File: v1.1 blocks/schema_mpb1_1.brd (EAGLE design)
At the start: 70.8 x 85.3 mm, 78 parts, among them IC1 CP2102, Q1 8M, Q2 32.768kHz, U1 NCP1117ST33T3G, U2 NCP1117ST50T3G, X2 PN61729-S, X5 POWERSUPPLY_DC21MMX

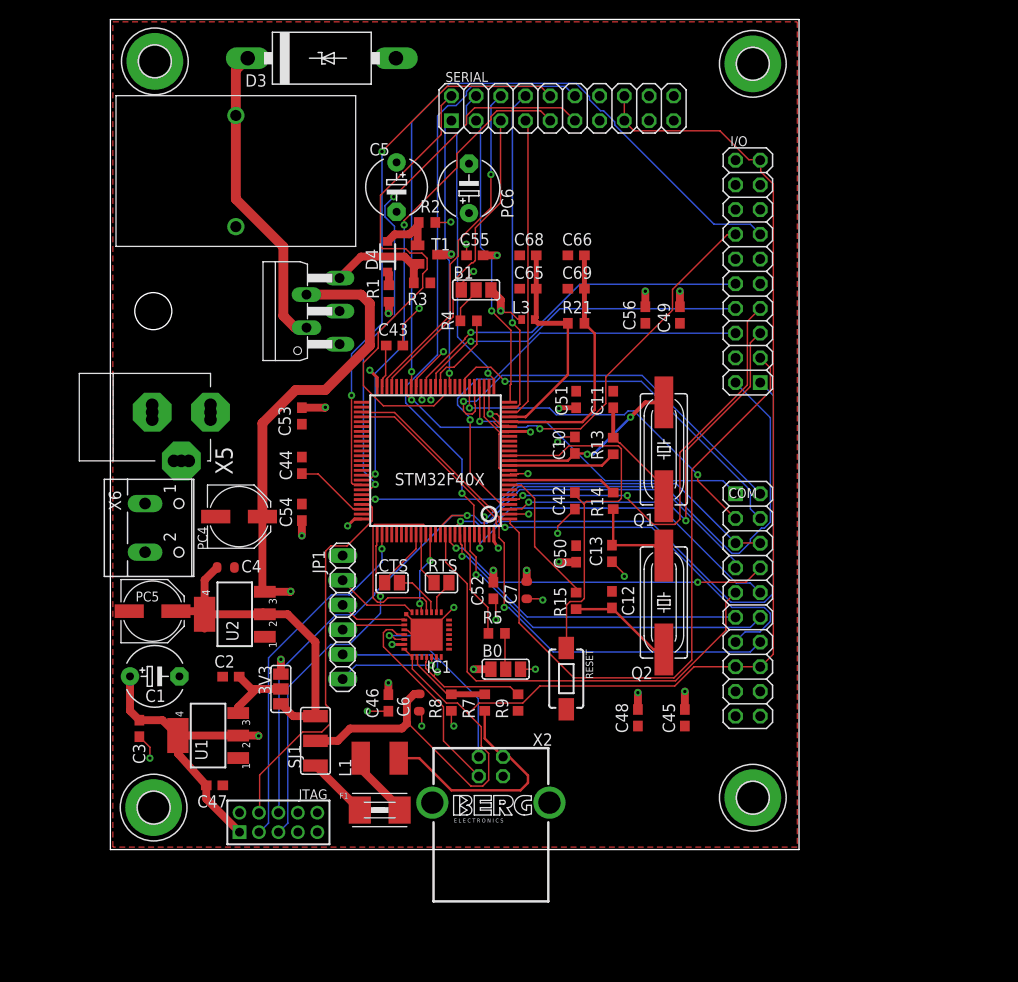
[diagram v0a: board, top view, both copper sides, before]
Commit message: Orientation
Changed board orientation to horizontal
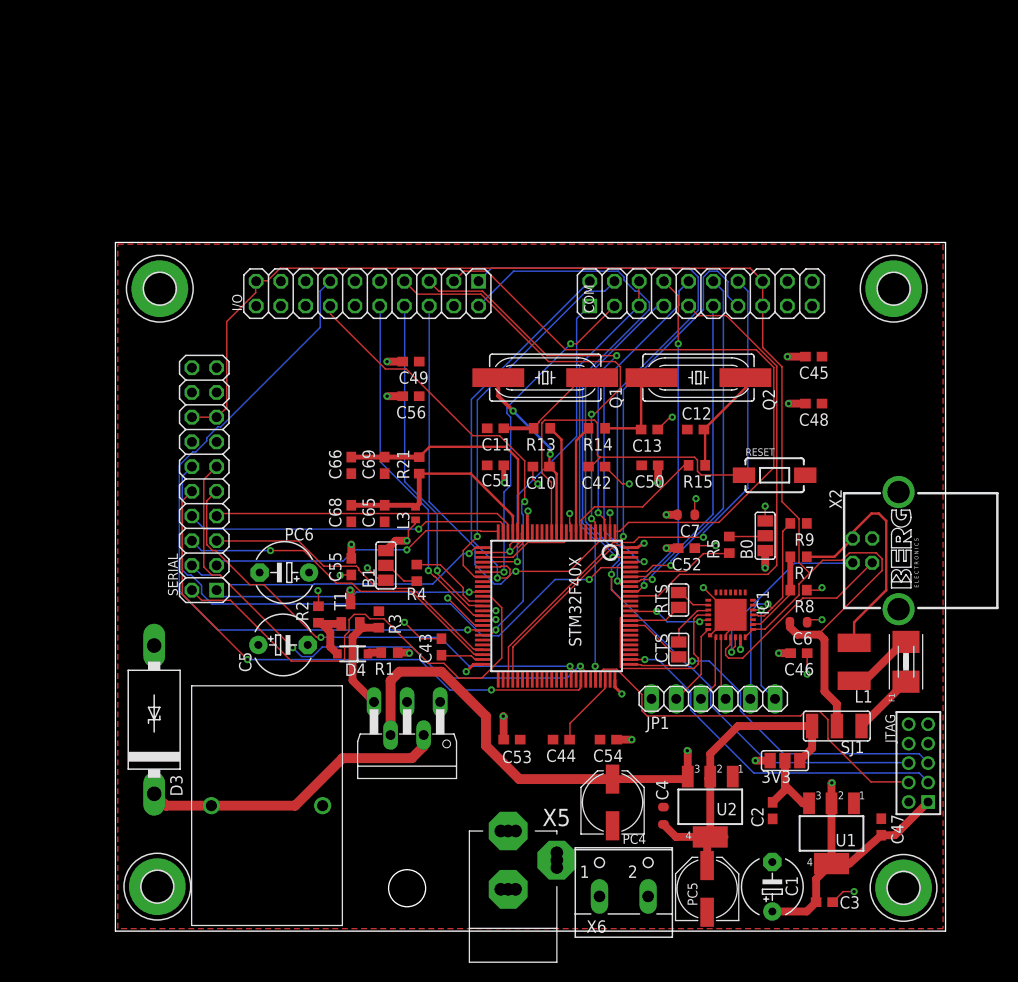
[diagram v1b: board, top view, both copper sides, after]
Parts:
- moved H2 84.8 mm to (4.57, 4.83), turned to 90 degrees
- moved H1 77.5 mm to (81.3, 4.70), turned to 90 degrees
- moved C3 72.6 mm to (73.1, 3.23), turned to 0 degrees
- moved D3 70.1 mm to (4.25, 22.0), turned to 90 degrees
- moved C47 68.7 mm to (79.0, 11.0), turned to 90 degrees
- moved C1 67.1 mm to (67.8, 4.81), turned to 90 degrees
- moved JTAG 66.1 mm to (82.8, 17.5), turned to 90 degrees
- moved L2 65.3 mm to (15.8, 13.2), turned to 0 degrees
- moved H3 65.2 mm to (4.83, 66.3), turned to 90 degrees
- moved U1 64.9 mm to (73.9, 10.3), turned to 180 degrees
- moved PC5 63.8 mm to (61.1, 4.59), turned to 90 degrees
- moved X5 61.7 mm to (40.6, 4.20), turned to 180 degrees
- moved X6 60.3 mm to (52.5, 5.09), turned to 0 degrees
- moved C2 57.4 mm to (67.8, 12.6), turned to 270 degrees
- moved F1 56.2 mm to (81.5, 27.9), turned to 90 degrees
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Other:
- board size 70.8 x 85.3 mm -> 85.3 x 70.8 mm

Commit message: First Revision
- Added 3 PIN terminal block for power
- Cleaned up tracks /rerouted
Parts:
- added X1: (no value), con-wago-500:W237-103
- moved H3 15.8 mm to (-6.10, 77.7)
- moved I/O 3.05 mm to (29.2, 65.8)
- moved D3 2.30 mm to (4.50, 19.7)
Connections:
- net +12V: now also X1.3
- net GND: now also X1.2
- net VIN: now also X1.1
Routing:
- net +12V: track 131.8 -> 194.4 mm
- net PE12: track 71.5 -> 43.6 mm
- net PE1: track 52.7 -> 31.0 mm
- net PE0: track 59.1 -> 40.0 mm
- net +5V: track 146.5 -> 128.5 mm, vias 0 -> 1
- net VIN: track 34.7 -> 46.3 mm
- net USB_OTG_HS_DM: track 56.2 -> 48.4 mm
- net REG_5V: track 34.6 -> 39.2 mm
- net ETH_MISO: track 34.9 -> 39.3 mm
- net RX5: track 57.0 -> 59.9 mm
- net 3.3V: track 77.7 -> 80.0 mm
- net N$14: track 21.3 -> 23.4 mm, vias 0 -> 1
- net PE13: track 47.4 -> 45.5 mm
- net PE3: track 29.9 -> 28.1 mm, vias 1 -> 2
- net PE6: track 44.4 -> 42.7 mm
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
